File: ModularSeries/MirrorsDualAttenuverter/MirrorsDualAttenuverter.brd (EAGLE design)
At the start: 46 x 49 mm, 37 parts, among them IC2 LM358

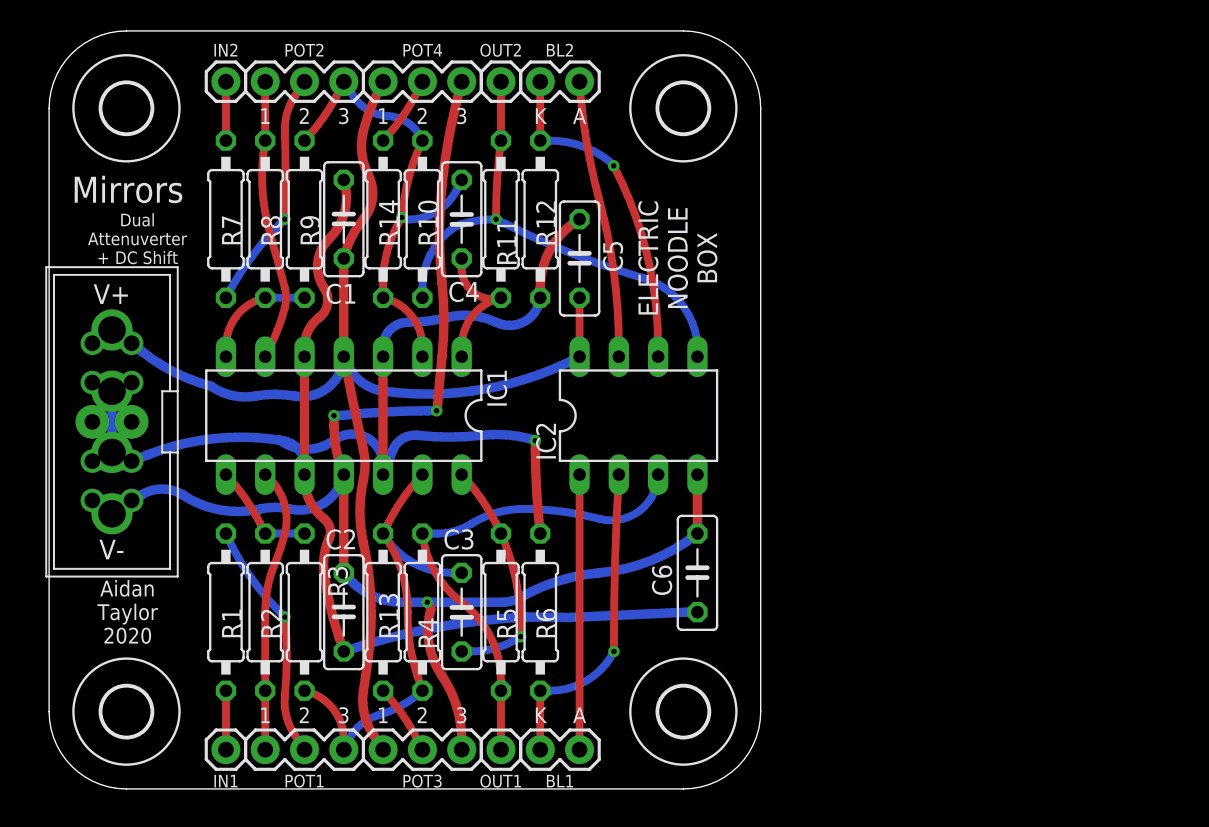
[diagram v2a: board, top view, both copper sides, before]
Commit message: TRHP-SVG version 2, Endings added and Mirrors updated
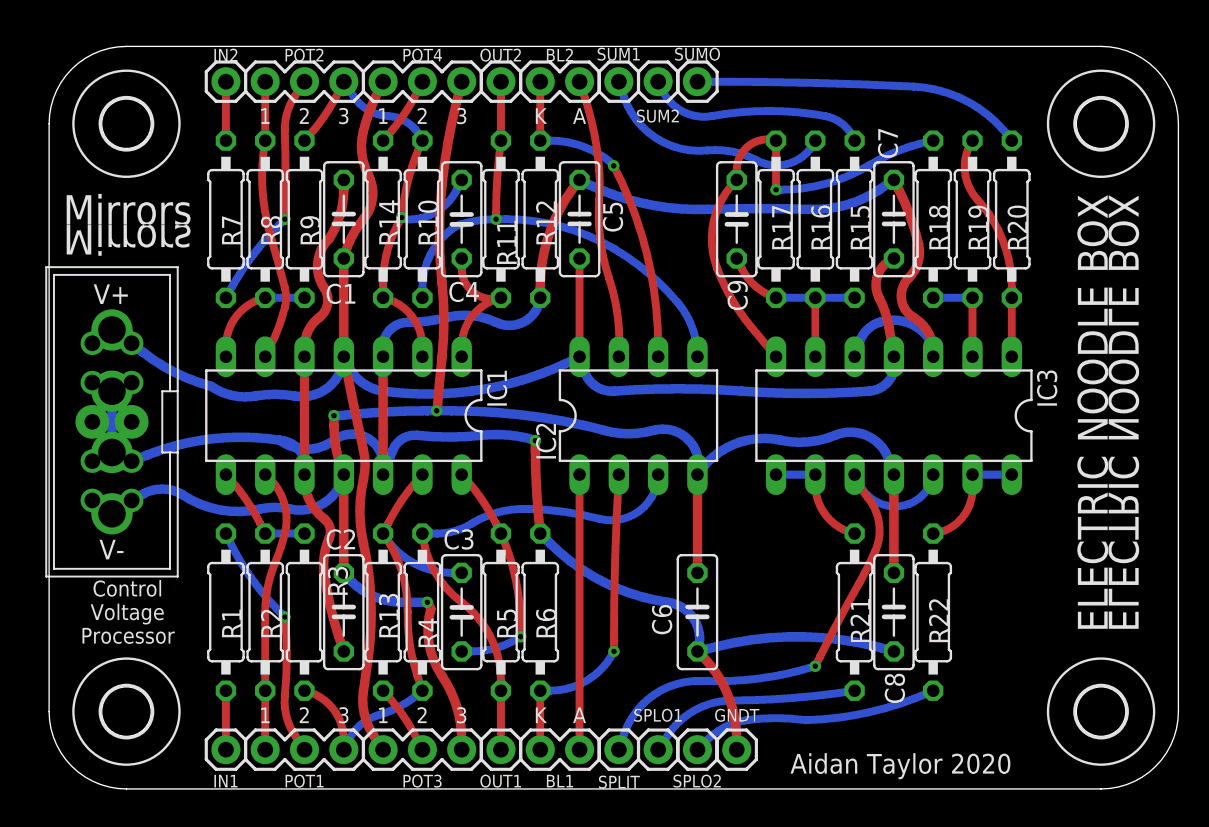
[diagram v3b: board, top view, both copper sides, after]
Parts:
- added C7, C8: 100nF, rcl:C050-025X075
- added C9: 22pF, rcl:C050-025X075
- added GNDT, SPLIT, SPLO1, SPLO2, SUM1, SUM2, SUMO: 1XWIREPAD, ElectricNoodleBox:1X01
- added IC3: (no value), ElectricNoodleBox:DIL14
- added R15, R16, R17, R18, R19: 100K, rcl:0207/10
- added R20, R21, R22: 100Ω, rcl:0207/10
- moved H2 27.0 mm to (68.0, 43.0)
- moved H1 27.0 mm to (68.0, 5.00)
- moved C6 2.54 mm to (41.9, 11.4)
- moved C5 2.54 mm to (34.3, 36.8)
- moved H3 1.00 mm to (5.00, 43.0)
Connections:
- new net N$10: IC3.2, R18.2, R19.1
- new net N$21: C9.2, IC3.6, R15.2, R16.2, R17.1
- new net N$23: C9.1, IC3.7, R17.2, R18.1
- new net N$24: IC3.1, R19.2, R20.1
- new net N$25: R20.2, SUMO.1
- new net N$26: R16.1, SUM1.1
- new net N$27: R15.1, SUM2.1
- new net N$28: IC3.8, IC3.9, R21.1
- new net N$29: IC3.13, IC3.14, R22.1
- new net N$30: IC3.10, IC3.12, SPLIT.1
- new net N$31: R21.2, SPLO1.1
- new net N$32: R22.2, SPLO2.1
- net +12V: now also C7.1, IC3.4
- net -12V: now also C8.2, IC3.11
- net AGND: now also C7.2, C8.1, GNDT.1, IC3.3, IC3.5
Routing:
- net AGND: track 129.1 -> 181.6 mm
- net N$30: track 0.00 -> 34.7 mm, vias 0 -> 1
- net +12V: track 82.9 -> 114.7 mm
- net N$23: track 0.00 -> 30.4 mm, vias 0 -> 1
- net -12V: track 93.7 -> 116.6 mm
- net N$25: track 0.00 -> 21.2 mm
- net N$32: track 0.00 -> 16.0 mm
- net N$26: track 0.00 -> 14.7 mm
- net N$24: track 0.00 -> 14.4 mm
- net N$27: track 0.00 -> 14.0 mm
- net N$31: track 0.00 -> 13.8 mm
- net N$21: track 0.00 -> 12.5 mm
- net N$29: track 0.00 -> 7.32 mm
- net N$28: track 0.00 -> 7.24 mm
- net N$10: track 0.00 -> 6.35 mm
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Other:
- board size 46 x 49 mm -> 73 x 48 mm
- board text added: "Control Voltage Processor"
- board text removed: "Dual Attenuverter + DC Shift"

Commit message: Portals schematic renders brought up to date
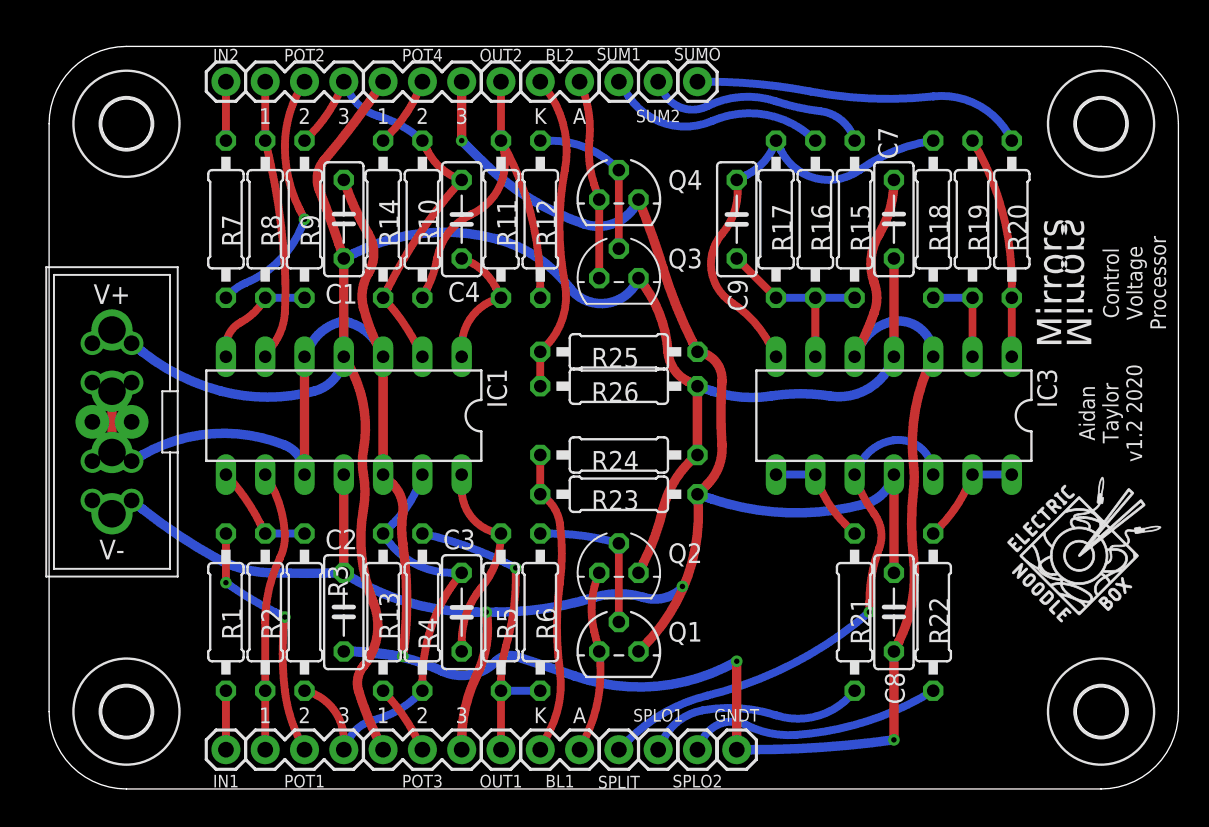
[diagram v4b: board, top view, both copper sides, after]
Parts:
- removed C5, C6: 100nF, rcl:C050-025X075
- removed IC2: LM358, ElectricNoodleBox:DIL08
- added Q1, Q4: 2N3906, transistor-pnp:TO92
- added Q2, Q3: 2N3904, transistor:TO92
- added R23, R24, R25, R26: 4K7, rcl:0207/10
- added U$1, U$2: (no value), ElectricNoodleBox:LOGO10X10
- R12, R6: value 1K -> 10K
- turned R12 to 90 degrees
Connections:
- new net N$33: BL1.2, R23.1, R24.2
- new net N$34: BL2.2, R25.1, R26.2
- net +12V: now also Q2.1, Q3.1, R24.1, R26.1; no longer C5.1, IC2.8
- net -12V: now also Q1.1, Q4.1, R23.2, R25.2; no longer C6.2, IC2.4
- net AGND: no longer C5.2, C6.1, R12.2, R6.2
- net N$14: now also R12.1; no longer IC2.5
- net N$17: now also Q3.2, Q4.2, R12.2; no longer BL2.1, IC2.7
- net N$18: now also BL2.1, Q3.3, Q4.3; no longer BL2.2, IC2.6, R12.1
- net N$19: now also BL1.1, Q1.3, Q2.3; no longer BL1.2, IC2.2, R6.1
- net N$6: now also R6.1; no longer IC2.3
- net N$8: now also Q1.2, Q2.2, R6.2; no longer BL1.1, IC2.1
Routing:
- net N$34: track 0.00 -> 20.2 mm
- net N$33: track 0.00 -> 19.6 mm
- net AGND: track 181.6 -> 166.3 mm, vias 1 -> 3
- net N$6: track 31.7 -> 20.8 mm, vias 0 -> 1
- net +12V: track 114.7 -> 125.1 mm
- net N$19: track 20.7 -> 11.6 mm, vias 1 -> 0
- net N$18: track 21.6 -> 12.8 mm, vias 1 -> 0
- net -12V: track 116.6 -> 124.8 mm
- net N$14: track 33.7 -> 25.8 mm, vias 1 -> 0
- net N$8: track 17.8 -> 10.2 mm
- net N$17: track 18.0 -> 10.6 mm
- net N$23: track 30.4 -> 27.4 mm, vias 1 -> 0
- net N$13: track 31.0 -> 28.4 mm, vias 1 -> 0
- net N$7: track 15.3 -> 12.8 mm, vias 1 -> 0
- net N$5: track 32.0 -> 29.6 mm
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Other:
- board text added: "Aidan Taylor v1.2 2020"
- board text removed: "Aidan Taylor 2020"
- board text removed: "ELECTRIC NOODLE BOX"
